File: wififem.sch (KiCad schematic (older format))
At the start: 31 parts, among them J1 Conn_Coaxial, J2 Conn_Coaxial, J3 Conn_Coaxial, J4 Conn_Coaxial, U1 MCP6566, U2 74HCT04, U3 SE2611T

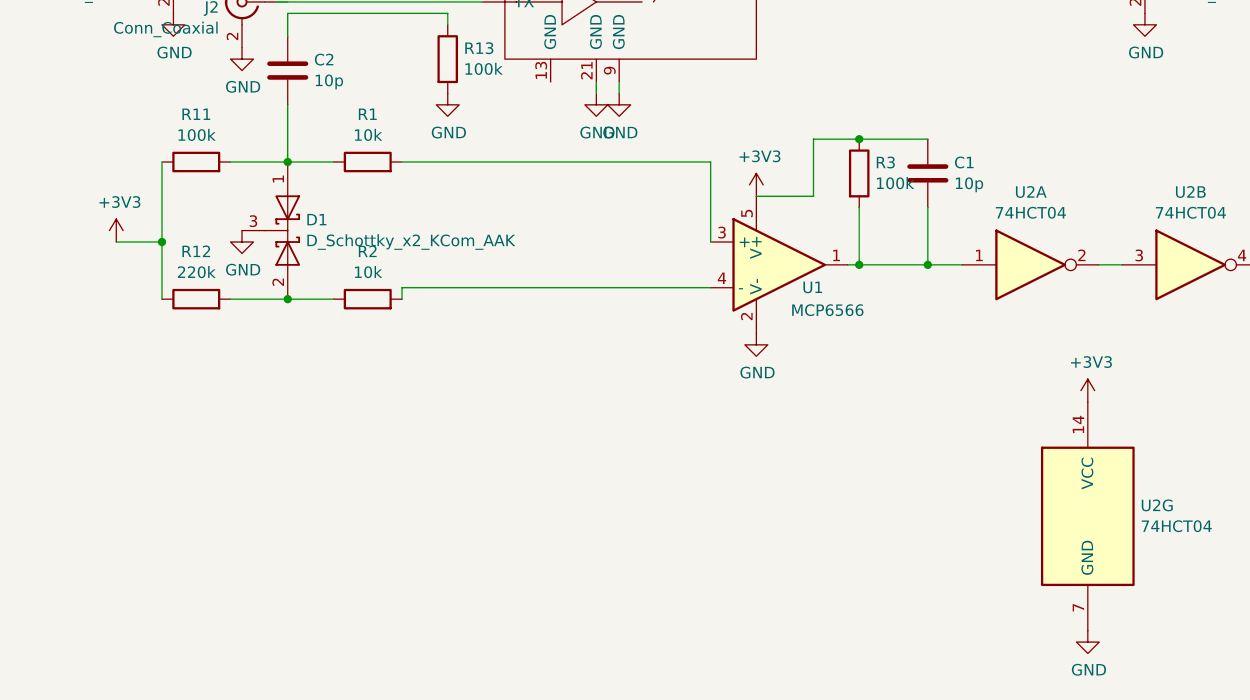
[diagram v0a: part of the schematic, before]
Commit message: Add regulator in schematic, some progress with layout
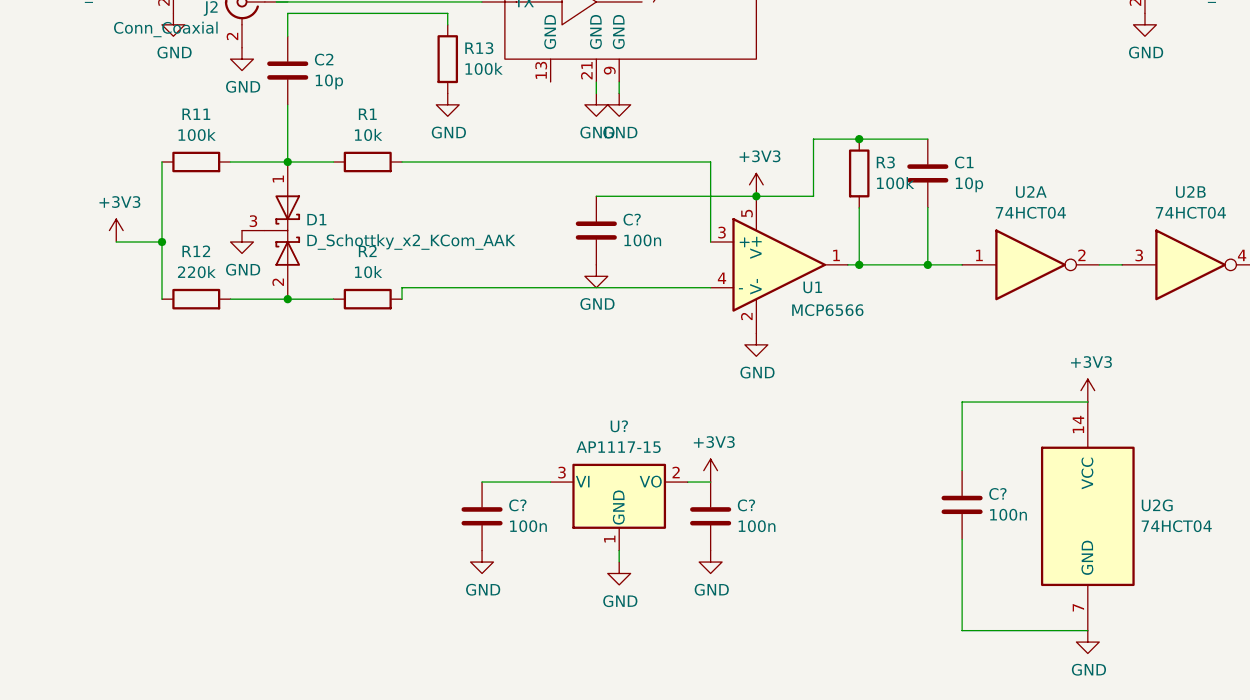
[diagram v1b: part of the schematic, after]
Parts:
- added C? (x4): 100n, Capacitors_SMD:C_0805_HandSoldering, symbol device:C
- added U?: AP1117-15, TO_SOT_Packages_SMD:SOT-223-3_TabPin2, symbol regul:AP1117-15
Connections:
- wire segments 65 -> 72
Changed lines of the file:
@@
 Connection ~ 6650 3400
 Wire Wire Line
-	6200 3650 6450 3650
+	5500 3650 6450 3650
 Wire Wire Line
 	6450 3400 6450 3650
@@
 Connection ~ 4150 4100
 Wire Wire Line
-	3600 4100 3600 3500
+	3600 3500 3600 4100
 $Comp
 L power:+3V3 #PWR019
@@
 	3400 3850 3600 3850
 Connection ~ 3600 3850
+$Comp
+L regul:AP1117-15 U?
+U 1 1 5A1A47EC
+P 5600 4900
+F 0 "U?" H 5600 5142 50  0000 C CNN
+F 1 "AP1117-15" H 5600 5051 50  0000 C CNN
+F 2 "TO_SOT_Packages_SMD:SOT-223-3_TabPin2" H 5600 5100 50  0001 C CNN
+F 3 "http://www.diodes.com/datasheets/AP1117.pdf" H 5700 4650 50  0001 C CNN
+	1    5600 4900
+	1    0    0    -1
+$EndComp
+$Comp
+L power:+3V3 #PWR?
+U 1 1 5A1A48D5
+P 6000 4900
+F 0 "#PWR?" H 6000 4750 50  0001 C CNN
+F 1 "+3V3" H 6015 5073 50  0000 C CNN
+F 2 "" H 6000 4900 50  0001 C CNN
+F 3 "" H 6000 4900 50  0001 C CNN
+	1    6000 4900
+	1    0    0    -1
+$EndComp
+Wire Wire Line
+	6000 4900 5900 4900
+$Comp
+L power:GND #PWR?
+U 1 1 5A1A6D47
+P 5600 5250
+F 0 "#PWR?" H 5600 5000 50  0001 C CNN
+F 1 "GND" H 5605 5077 50  0000 C CNN
+F 2 "" H 5600 5250 50  0001 C CNN
+F 3 "" H 5600 5250 50  0001 C CNN
+	1    5600 5250
+	1    0    0    -1
+$EndComp
+Wire Wire Line
+	5600 5250 5600 5200
+$Comp
+L device:C C?
+U 1 1 5A1AA377
+P 6000 5050
+F 0 "C?" H 5885 5004 50  0000 R CNN
+F 1 "100n" H 5885 5095 50  0000 R CNN
+F 2 "Capacitors_SMD:C_0805_HandSoldering" H 6038 4900 50  0001 C CNN
+F 3 "" H 6000 5050 50  0001 C CNN
+	1    6000 5050
+	-1   0    0    1
+$EndComp
+$Comp
+L power:GND #PWR?
+U 1 1 5A1AA62D
+P 6000 5200
+F 0 "#PWR?" H 6000 4950 50  0001 C CNN
+F 1 "GND" H 6005 5027 50  0000 C CNN
+F 2 "" H 6000 5200 50  0001 C CNN
+F 3 "" H 6000 5200 50  0001 C CNN
+	1    6000 5200
+	1    0    0    -1
+$EndComp
+$Comp
+L device:C C?
+U 1 1 5A1AA680
+P 5000 5050
+F 0 "C?" H 4885 5004 50  0000 R CNN
+F 1 "100n" H 4885 5095 50  0000 R CNN
+F 2 "Capacitors_SMD:C_0805_HandSoldering" H 5038 4900 50  0001 C CNN
+F 3 "" H 5000 5050 50  0001 C CNN
+	1    5000 5050
+	-1   0    0    1
+$EndComp
+Wire Wire Line
+	5300 4900 5000 4900
+$Comp
+L power:GND #PWR?
+U 1 1 5A1ACCE4
+P 5000 5200
+F 0 "#PWR?" H 5000 4950 50  0001 C CNN
+F 1 "GND" H 5005 5027 50  0000 C CNN
+F 2 "" H 5000 5200 50  0001 C CNN
+F 3 "" H 5000 5200 50  0001 C CNN
+	1    5000 5200
+	1    0    0    -1
+$EndComp
+$Comp
+L device:C C?
+U 1 1 5A1ACD39
+P 5500 3800
+F 0 "C?" H 5385 3754 50  0000 R CNN
+F 1 "100n" H 5385 3845 50  0000 R CNN
+F 2 "Capacitors_SMD:C_0805_HandSoldering" H 5538 3650 50  0001 C CNN
+F 3 "" H 5500 3800 50  0001 C CNN
+	1    5500 3800
+	-1   0    0    1
+$EndComp
+Connection ~ 6200 3650
+$Comp
+L power:GND #PWR?
+U 1 1 5A1B10BA
+P 5500 3950
+F 0 "#PWR?" H 5500 3700 50  0001 C CNN
+F 1 "GND" H 5505 3777 50  0000 C CNN
+F 2 "" H 5500 3950 50  0001 C CNN
+F 3 "" H 5500 3950 50  0001 C CNN
+	1    5500 3950
+	1    0    0    -1
+$EndComp
+$Comp
+L device:C C?
+U 1 1 5A1B1111
+P 7100 5000
+F 0 "C?" H 6985 4954 50  0000 R CNN
+F 1 "100n" H 6985 5045 50  0000 R CNN
+F 2 "Capacitors_SMD:C_0805_HandSoldering" H 7138 4850 50  0001 C CNN
+F 3 "" H 7100 5000 50  0001 C CNN
+	1    7100 5000
+	-1   0    0    1
+$EndComp
+Wire Wire Line
+	7650 4550 7100 4550
+Wire Wire Line
+	7100 4550 7100 4850
+Wire Wire Line
+	7650 5550 7100 5550
+Wire Wire Line
+	7100 5550 7100 5150
 $EndSCHEMATC
